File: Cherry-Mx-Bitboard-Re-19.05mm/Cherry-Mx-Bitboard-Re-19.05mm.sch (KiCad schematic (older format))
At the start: 11 parts, among them SW1 SW_Push

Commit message: added choc
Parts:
- added D3, D4: 1N4148W-Diode, Footprints:1N4148W, symbol Cherry-Mx-Bitboard-Re-19.05mm-rescue:1N4148W-Diode
- added SW2: SW_Push-Switch, keyswitches:Kailh_socket_PG1350, symbol Cherry-Mx-Bitboard-Re-19.05mm-rescue:SW_Push-Switch
- Col111, Col112, Col113, Col114, Row111, Row112, Row113, Row114: symbol Connector_Generic:Conn_01x01 -> Cherry-Mx-Bitboard-Re-19.05mm-rescue:Conn_01x01-Connector_Generic
- D1, D2: symbol Diode:1N4148W -> Cherry-Mx-Bitboard-Re-19.05mm-rescue:1N4148W-Diode
- SW1: symbol Switch:SW_Push -> Cherry-Mx-Bitboard-Re-19.05mm-rescue:SW_Push-Switch
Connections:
- wire segments 22 -> 33
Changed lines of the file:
@@
 EESchema Schematic File Version 4
-LIBS:Cherry-Mx-Bitboard-Re-19.05mm-cache
 EELAYER 30 0
 EELAYER END
@@
 $EndDescr
 $Comp
-L Switch:SW_Push SW1
+L Cherry-Mx-Bitboard-Re-19.05mm-rescue:SW_Push-Switch SW1
 U 1 1 5B598EC8
 P 2000 4500
@@
 	1750 4500 1750 4600
 $Comp
-L Connector_Generic:Conn_01x01 Col111
+L Cherry-Mx-Bitboard-Re-19.05mm-rescue:Conn_01x01-Connector_Generic Col111
 U 1 1 5B8A669A
 P 9450 2800
@@
 $EndComp
 $Comp
-L Diode:1N4148W D1
+L Cherry-Mx-Bitboard-Re-19.05mm-rescue:1N4148W-Diode D1
 U 1 1 5B954373
 P 2400 4500
@@
 Row1
 $Comp
-L Connector_Generic:Conn_01x01 Row112
+L Cherry-Mx-Bitboard-Re-19.05mm-rescue:Conn_01x01-Connector_Generic Row112
 U 1 1 5B8A9836
 P 9150 3300
@@
 Row1
 $Comp
-L Connector_Generic:Conn_01x01 Row113
+L Cherry-Mx-Bitboard-Re-19.05mm-rescue:Conn_01x01-Connector_Generic Row113
 U 1 1 5BCDE34F
 P 9950 3100
@@
 $EndComp
 $Comp
-L Connector_Generic:Conn_01x01 Row114
+L Cherry-Mx-Bitboard-Re-19.05mm-rescue:Conn_01x01-Connector_Generic Row114
 U 1 1 5BCDE64E
 P 9950 3300
@@
 $EndComp
 $Comp
-L Connector_Generic:Conn_01x01 Col112
+L Cherry-Mx-Bitboard-Re-19.05mm-rescue:Conn_01x01-Connector_Generic Col112
 U 1 1 5BCE08C8
 P 9650 2800
@@
 Col1
 $Comp
-L Connector_Generic:Conn_01x01 Col113
+L Cherry-Mx-Bitboard-Re-19.05mm-rescue:Conn_01x01-Connector_Generic Col113
 U 1 1 5BD12023
 P 9450 3600
@@
 $EndComp
 $Comp
-L Connector_Generic:Conn_01x01 Col114
+L Cherry-Mx-Bitboard-Re-19.05mm-rescue:Conn_01x01-Connector_Generic Col114
 U 1 1 5BD1233F
 P 9650 3600
@@
 	9350 3200 9750 3200
 $Comp
-L Connector_Generic:Conn_01x01 Row111
+L Cherry-Mx-Bitboard-Re-19.05mm-rescue:Conn_01x01-Connector_Generic Row111
 U 1 1 5B8A59A9
 P 9150 3100
@@
 	2200 4900 2250 4900
 $Comp
-L Diode:1N4148W D2
+L Cherry-Mx-Bitboard-Re-19.05mm-rescue:1N4148W-Diode D2
 U 1 1 5E1FCD4B
 P 2400 4900
@@
 	2550 4900 2750 4900
 Wire Wire Line
-	2200 4900 2200 4500
+	2200 4900 2200 4700
 Connection ~ 2200 4500
 Wire Wire Line
 	2750 4900 2750 4500
 Connection ~ 2750 4500
+$Comp
+L Cherry-Mx-Bitboard-Re-19.05mm-rescue:SW_Push-Switch SW2
+U 1 1 5EAC5567
+P 2000 4700
+F 0 "SW2" H 2000 4985 50  0000 C CNN
+F 1 "SW_Push-Switch" H 2000 4894 50  0000 C CNN
+F 2 "keyswitches:Kailh_socket_PG1350" H 2000 4900 50  0001 C CNN
+F 3 "" H 2000 4900 50  0001 C CNN
+	1    2000 4700
+	1    0    0    -1
+$EndComp
+Connection ~ 2200 4700
+Wire Wire Line
+	2200 4700 2200 4500
+Wire Wire Line
+	1800 4700 1750 4700
+Wire Wire Line
+	1750 4700 1750 4600
+Connection ~ 1750 4600
+$Comp
+L Cherry-Mx-Bitboard-Re-19.05mm-rescue:1N4148W-Diode D3
+U 1 1 5EAE37ED
+P 2400 5250
+F 0 "D3" H 2400 5467 50  0000 C CNN
+F 1 "1N4148W-Diode" H 2400 5376 50  0000 C CNN
+F 2 "Footprints:1N4148W" H 2400 5075 50  0001 C CNN
+F 3 "" H 2400 5250 50  0001 C CNN
+	1    2400 5250
+	-1   0    0    -1
+$EndComp
+Wire Wire Line
+	2550 5250 2750 5250
+Wire Wire Line
+	2750 5250 2750 4900
+Connection ~ 2750 4900
+Wire Wire Line
+	2250 5250 2200 5250
+Wire Wire Line
+	2200 5250 2200 4900
+Connection ~ 2200 4900
+$Comp
+L Cherry-Mx-Bitboard-Re-19.05mm-rescue:1N4148W-Diode D4
+U 1 1 5EAE84E4
+P 2400 5600
+F 0 "D4" H 2400 5817 50  0000 C CNN
+F 1 "1N4148W-Diode" H 2400 5726 50  0000 C CNN
+F 2 "Footprints:1N4148W" H 2400 5425 50  0001 C CNN
+F 3 "" H 2400 5600 50  0001 C CNN
+	1    2400 5600
+	-1   0    0    -1
+$EndComp
+Wire Wire Line
+	2550 5600 2750 5600
+Wire Wire Line
+	2750 5600 2750 5250
+Connection ~ 2750 5250
+Wire Wire Line
+	2250 5600 2200 5600
+Wire Wire Line
+	2200 5600 2200 5250
+Connection ~ 2200 5250
 $EndSCHEMATC

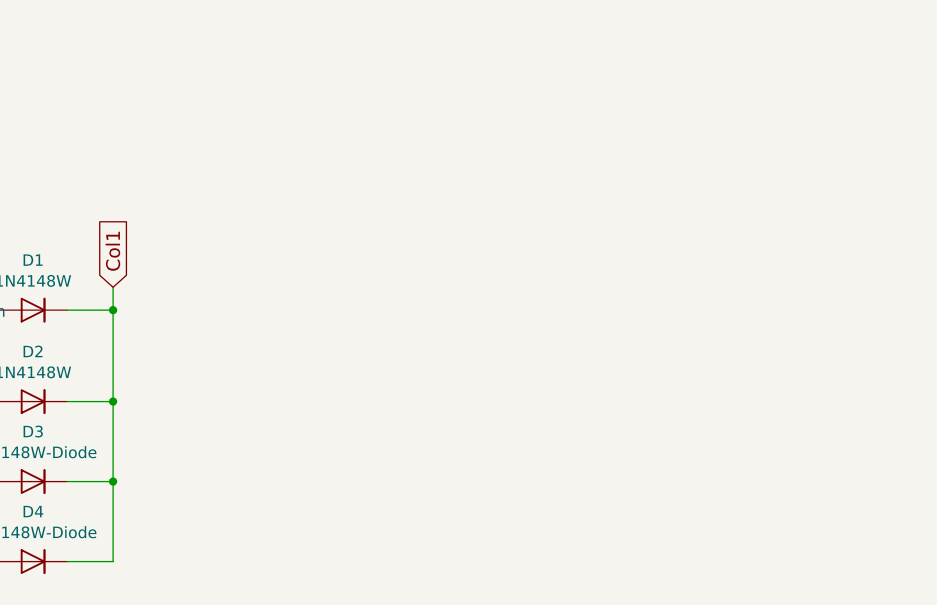
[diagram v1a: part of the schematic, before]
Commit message: add rgb leds
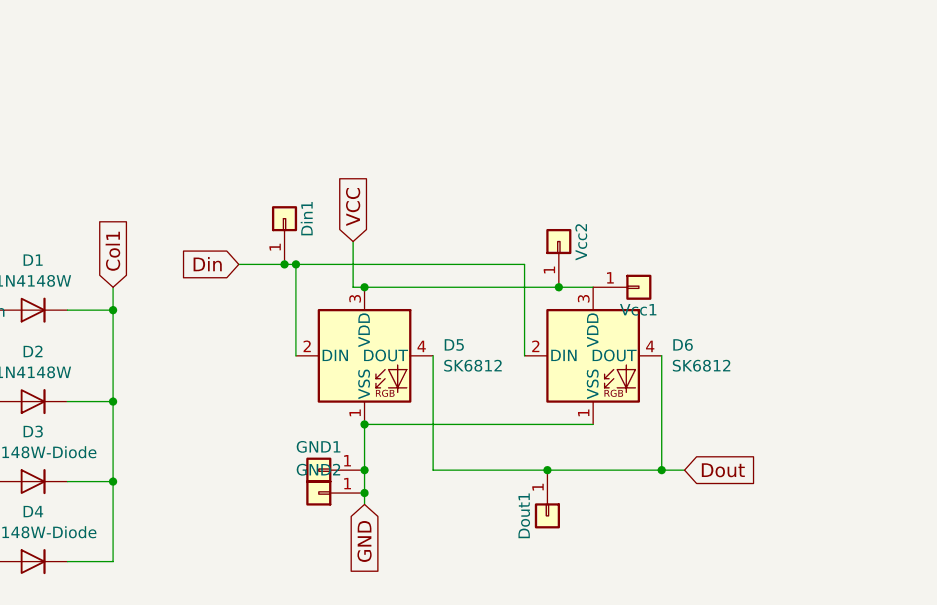
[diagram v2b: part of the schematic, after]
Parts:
- added D5, D6: SK6812, LED_SMD:LED_SK6812_PLCC4_5.0x5.0mm_P3.2mm, symbol LED:SK6812
- added Din1, Dout1, GND1, GND2, Vcc1, Vcc2: Conn_01x01, Footprints:Wirepad, symbol Cherry-Mx-Bitboard-Re-19.05mm-rescue:Conn_01x01-Connector_Generic
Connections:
- new net Din: D5.2 (DIN), D6.2 (DIN), Din1.1 (Pin_1)
- new net Dout: D5.4 (DOUT), D6.4 (DOUT), Dout1.1 (Pin_1)
- new net GND: D5.1 (VSS), D6.1 (VSS), GND1.1 (Pin_1), GND2.1 (Pin_1)
- new net VCC: D5.3 (VDD), D6.3 (VDD), Vcc1.1 (Pin_1), Vcc2.1 (Pin_1)
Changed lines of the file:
@@
 	2200 5600 2200 5250
 Connection ~ 2200 5250
+$Comp
+L LED:SK6812 D5
+U 1 1 5EB32545
+P 3850 4700
+F 0 "D5" H 4194 4746 50  0000 L CNN
+F 1 "SK6812" H 4194 4655 50  0000 L CNN
+F 2 "LED_SMD:LED_SK6812_PLCC4_5.0x5.0mm_P3.2mm" H 3900 4400 50  0001 L TNN
+F 3 "https://cdn-shop.adafruit.com/product-files/1138/SK6812+LED+datasheet+.pdf" H 3950 4325 50  0001 L TNN
+	1    3850 4700
+	1    0    0    -1
+$EndComp
+Text GLabel 3800 4200 1    60   Input ~ 0
+VCC
+Text GLabel 3850 5350 3    60   Input ~ 0
+GND
+Text GLabel 3300 4300 0    60   Input ~ 0
+Din
+Text GLabel 5250 5200 2    60   Input ~ 0
+Dout
+$Comp
+L LED:SK6812 D6
+U 1 1 5EB36B3B
+P 4850 4700
+F 0 "D6" H 5194 4746 50  0000 L CNN
+F 1 "SK6812" H 5194 4655 50  0000 L CNN
+F 2 "LED_SMD:LED_SK6812_PLCC4_5.0x5.0mm_P3.2mm" H 4900 4400 50  0001 L TNN
+F 3 "https://cdn-shop.adafruit.com/product-files/1138/SK6812+LED+datasheet+.pdf" H 4950 4325 50  0001 L TNN
+	1    4850 4700
+	1    0    0    -1
+$EndComp
+Wire Wire Line
+	3800 4200 3800 4400
+Wire Wire Line
+	3800 4400 3850 4400
+Wire Wire Line
+	4850 4400 4700 4400
+Connection ~ 3850 4400
+Wire Wire Line
+	3850 5000 4850 5000
+Wire Wire Line
+	3850 5350 3850 5300
+Connection ~ 3850 5000
+Wire Wire Line
+	3550 4300 3550 4700
+Wire Wire Line
+	3550 4300 4550 4300
+Wire Wire Line
+	4550 4300 4550 4700
+Connection ~ 3550 4300
+Wire Wire Line
+	5150 4700 5150 5200
+Wire Wire Line
+	5150 5200 5250 5200
+Wire Wire Line
+	4150 4700 4150 5200
+Wire Wire Line
+	4150 5200 4650 5200
+Connection ~ 5150 5200
+$Comp
+L Cherry-Mx-Bitboard-Re-19.05mm-rescue:Conn_01x01-Connector_Generic Din1
+U 1 1 5EB414D3
+P 3500 4100
+F 0 "Din1" H 3500 4000 50  0000 C CNN
+F 1 "Conn_01x01" V 3375 4012 50  0001 R CNN
+F 2 "Footprints:Wirepad" H 3500 4100 50  0001 C CNN
+F 3 "~" H 3500 4100 50  0001 C CNN
+	1    3500 4100
+	0    -1   -1   0
+$EndComp
+$Comp
+L Cherry-Mx-Bitboard-Re-19.05mm-rescue:Conn_01x01-Connector_Generic Dout1
+U 1 1 5EB42BEB
+P 4650 5400
+F 0 "Dout1" H 4650 5300 50  0000 C CNN
+F 1 "Conn_01x01" V 4525 5312 50  0001 R CNN
+F 2 "Footprints:Wirepad" H 4650 5400 50  0001 C CNN
+F 3 "~" H 4650 5400 50  0001 C CNN
+	1    4650 5400
+	0    1    1    0
+$EndComp
+$Comp
+L Cherry-Mx-Bitboard-Re-19.05mm-rescue:Conn_01x01-Connector_Generic GND1
+U 1 1 5EB43F3B
+P 3650 5200
+F 0 "GND1" H 3650 5100 50  0000 C CNN
+F 1 "Conn_01x01" V 3525 5112 50  0001 R CNN
+F 2 "Footprints:Wirepad" H 3650 5200 50  0001 C CNN
+F 3 "~" H 3650 5200 50  0001 C CNN
+	1    3650 5200
+	-1   0    0    1
+$EndComp
+$Comp
+L Cherry-Mx-Bitboard-Re-19.05mm-rescue:Conn_01x01-Connector_Generic Vcc1
+U 1 1 5EB45E0D
+P 5050 4400
+F 0 "Vcc1" H 5050 4300 50  0000 C CNN
+F 1 "Conn_01x01" V 4925 4312 50  0001 R CNN
+F 2 "Footprints:Wirepad" H 5050 4400 50  0001 C CNN
+F 3 "~" H 5050 4400 50  0001 C CNN
+	1    5050 4400
+	1    0    0    -1
+$EndComp
+Connection ~ 3850 5200
+Wire Wire Line
+	3850 5200 3850 5000
+Connection ~ 4650 5200
+Wire Wire Line
+	4650 5200 5150 5200
+Wire Wire Line
+	3500 4300 3550 4300
+Wire Wire Line
+	3500 4300 3300 4300
+Connection ~ 3500 4300
+$Comp
+L Cherry-Mx-Bitboard-Re-19.05mm-rescue:Conn_01x01-Connector_Generic GND2
+U 1 1 5EB66F22
+P 3650 5300
+F 0 "GND2" H 3650 5200 50  0000 C CNN
+F 1 "Conn_01x01" V 3525 5212 50  0001 R CNN
+F 2 "Footprints:Wirepad" H 3650 5300 50  0001 C CNN
+F 3 "~" H 3650 5300 50  0001 C CNN
+	1    3650 5300
+	-1   0    0    1
+$EndComp
+$Comp
+L Cherry-Mx-Bitboard-Re-19.05mm-rescue:Conn_01x01-Connector_Generic Vcc2
+U 1 1 5EB69C64
+P 4700 4200
+F 0 "Vcc2" H 4700 4100 50  0000 C CNN
+F 1 "Conn_01x01" V 4575 4112 50  0001 R CNN
+F 2 "Footprints:Wirepad" H 4700 4200 50  0001 C CNN
+F 3 "~" H 4700 4200 50  0001 C CNN
+	1    4700 4200
+	0    -1   -1   0
+$EndComp
+Connection ~ 4700 4400
+Wire Wire Line
+	4700 4400 3850 4400
+Connection ~ 3850 5300
+Wire Wire Line
+	3850 5300 3850 5200
 $EndSCHEMATC

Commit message: simplified
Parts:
- removed D3, D4: 1N4148W-Diode, Footprints:1N4148W, symbol Cherry-Mx-Bitboard-Re-19.05mm-rescue:1N4148W-Diode
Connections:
- net Row1: now also SW1.2, SW2.2; no longer SW1.1, SW2.1
- net at D1.2 (A), D2.2 (A): now also SW1.1, SW2.1; no longer SW1.2, SW2.2
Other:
- moved on the sheet: SW1, SW2
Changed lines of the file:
@@
 L Cherry-Mx-Bitboard-Re-19.05mm-rescue:SW_Push-Switch SW1
 U 1 1 5B598EC8
-P 2000 4500
-F 0 "SW1" H 2000 4785 50  0000 C CNN
-F 1 "SW_Push" H 2000 4694 50  0000 C CNN
-F 2 "Footprints:CherryMx_Socket" H 2000 4700 50  0001 C CNN
-F 3 "" H 2000 4700 50  0001 C CNN
-	1    2000 4500
+P 1800 4350
+F 0 "SW1" H 1800 4635 50  0000 C CNN
+F 1 "SW_Push" H 1800 4544 50  0000 C CNN
+F 2 "Footprints:CherryMx_Socket" H 1800 4550 50  0001 C CNN
+F 3 "" H 1800 4550 50  0001 C CNN
+	1    1800 4350
 	1    0    0    -1
 $EndComp
 Wire Wire Line
 	2200 4500 2250 4500
-Wire Wire Line
-	1800 4500 1750 4500
 Wire Wire Line
 	1750 4500 1750 4600
@@
 	2550 4900 2750 4900
 Wire Wire Line
-	2200 4900 2200 4700
-Connection ~ 2200 4500
-Wire Wire Line
 	2750 4900 2750 4500
 Connection ~ 2750 4500
@@
 L Cherry-Mx-Bitboard-Re-19.05mm-rescue:SW_Push-Switch SW2
 U 1 1 5EAC5567
-P 2000 4700
-F 0 "SW2" H 2000 4985 50  0000 C CNN
-F 1 "SW_Push-Switch" H 2000 4894 50  0000 C CNN
-F 2 "keyswitches:Kailh_socket_PG1350" H 2000 4900 50  0001 C CNN
-F 3 "" H 2000 4900 50  0001 C CNN
-	1    2000 4700
-	1    0    0    -1
-$EndComp
-Connection ~ 2200 4700
-Wire Wire Line
-	2200 4700 2200 4500
-Wire Wire Line
-	1800 4700 1750 4700
+P 1800 4900
+F 0 "SW2" H 1800 5185 50  0000 C CNN
+F 1 "SW_Push-Switch" H 1800 5094 50  0000 C CNN
+F 2 "keyswitches:Kailh_socket_PG1350" H 1800 5100 50  0001 C CNN
+F 3 "" H 1800 5100 50  0001 C CNN
+	1    1800 4900
+	1    0    0    -1
+$EndComp
 Wire Wire Line
 	1750 4700 1750 4600
 Connection ~ 1750 4600
-$Comp
-L Cherry-Mx-Bitboard-Re-19.05mm-rescue:1N4148W-Diode D3
-U 1 1 5EAE37ED
-P 2400 5250
-F 0 "D3" H 2400 5467 50  0000 C CNN
-F 1 "1N4148W-Diode" H 2400 5376 50  0000 C CNN
-F 2 "Footprints:1N4148W" H 2400 5075 50  0001 C CNN
-F 3 "" H 2400 5250 50  0001 C CNN
-	1    2400 5250
-	-1   0    0    -1
-$EndComp
-Wire Wire Line
-	2550 5250 2750 5250
-Wire Wire Line
-	2750 5250 2750 4900
-Connection ~ 2750 4900
-Wire Wire Line
-	2250 5250 2200 5250
-Wire Wire Line
-	2200 5250 2200 4900
-Connection ~ 2200 4900
-$Comp
-L Cherry-Mx-Bitboard-Re-19.05mm-rescue:1N4148W-Diode D4
-U 1 1 5EAE84E4
-P 2400 5600
-F 0 "D4" H 2400 5817 50  0000 C CNN
-F 1 "1N4148W-Diode" H 2400 5726 50  0000 C CNN
-F 2 "Footprints:1N4148W" H 2400 5425 50  0001 C CNN
-F 3 "" H 2400 5600 50  0001 C CNN
-	1    2400 5600
-	-1   0    0    -1
-$EndComp
-Wire Wire Line
-	2550 5600 2750 5600
-Wire Wire Line
-	2750 5600 2750 5250
-Connection ~ 2750 5250
-Wire Wire Line
-	2250 5600 2200 5600
-Wire Wire Line
-	2200 5600 2200 5250
-Connection ~ 2200 5250
 $Comp
 L LED:SK6812 D5
@@
 Wire Wire Line
 	3850 5300 3850 5200
+Wire Wire Line
+	2200 4500 2200 4900
+Wire Wire Line
+	2200 4500 2200 4200
+Wire Wire Line
+	2200 4200 1600 4200
+Wire Wire Line
+	1600 4200 1600 4350
+Connection ~ 2200 4500
+Wire Wire Line
+	2000 4350 2000 4500
+Wire Wire Line
+	1750 4500 2000 4500
+Wire Wire Line
+	2000 4700 2000 4900
+Wire Wire Line
+	1750 4700 2000 4700
+Wire Wire Line
+	1600 4900 1600 5000
+Wire Wire Line
+	1600 5000 2200 5000
+Wire Wire Line
+	2200 5000 2200 4900
+Connection ~ 2200 4900
 $EndSCHEMATC

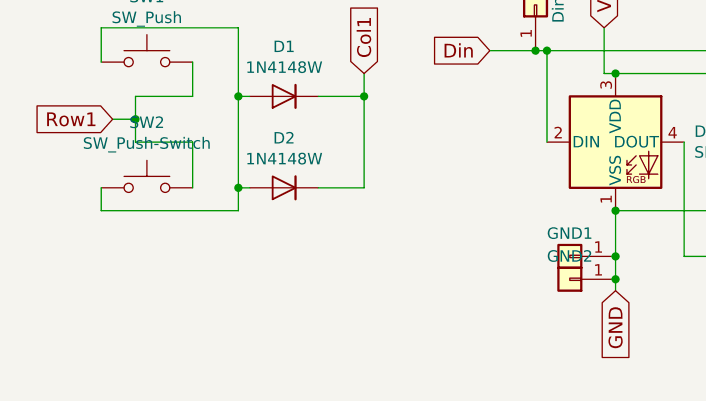
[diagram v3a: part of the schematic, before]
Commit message: fix both sides rgb leds
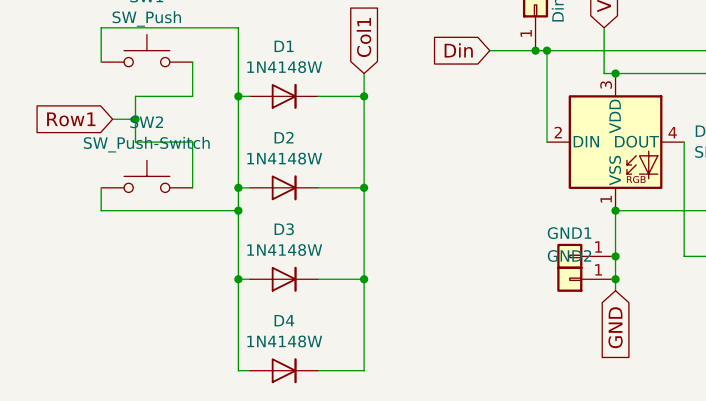
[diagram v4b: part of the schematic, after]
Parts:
- added D3, D4: 1N4148W, Footprints:1N4148W, symbol Cherry-Mx-Bitboard-Re-19.05mm-rescue:1N4148W-Diode
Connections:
- net Col1: now also D3.1 (K), D4.1 (K)
- net at D1.2 (A), D2.2 (A), SW1.1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: now also D3.2 (A), D4.2 (A)
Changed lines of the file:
@@
 	2200 5000 2200 4900
 Connection ~ 2200 4900
+$Comp
+L Cherry-Mx-Bitboard-Re-19.05mm-rescue:1N4148W-Diode D3
+U 1 1 5EB08F87
+P 2400 5300
+F 0 "D3" H 2400 5083 50  0000 C CNN
+F 1 "1N4148W" H 2400 5174 50  0000 C CNN
+F 2 "Footprints:1N4148W" H 2400 5125 50  0001 C CNN
+F 3 "https://www.vishay.com/docs/85748/1n4148w.pdf" H 2400 5300 50  0001 C CNN
+	1    2400 5300
+	-1   0    0    1
+$EndComp
+$Comp
+L Cherry-Mx-Bitboard-Re-19.05mm-rescue:1N4148W-Diode D4
+U 1 1 5EB08F8D
+P 2400 5700
+F 0 "D4" H 2400 5483 50  0000 C CNN
+F 1 "1N4148W" H 2400 5574 50  0000 C CNN
+F 2 "Footprints:1N4148W" H 2400 5525 50  0001 C CNN
+F 3 "https://www.vishay.com/docs/85748/1n4148w.pdf" H 2400 5700 50  0001 C CNN
+	1    2400 5700
+	-1   0    0    1
+$EndComp
+Wire Wire Line
+	2200 5300 2250 5300
+Connection ~ 2200 5000
+Wire Wire Line
+	2200 5000 2200 5300
+Wire Wire Line
+	2200 5300 2200 5700
+Wire Wire Line
+	2200 5700 2250 5700
+Connection ~ 2200 5300
+Wire Wire Line
+	2750 4900 2750 5300
+Wire Wire Line
+	2750 5300 2550 5300
+Connection ~ 2750 4900
+Wire Wire Line
+	2750 5300 2750 5700
+Wire Wire Line
+	2750 5700 2550 5700
+Connection ~ 2750 5300
 $EndSCHEMATC

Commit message: add custom footprint
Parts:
- D5, D6: footprint LED_SMD:LED_SK6812_PLCC4_5.0x5.0mm_P3.2mm -> customs:LED_SK6812_PLCC4_5.0x5.0mm_P3.2mm_FLIP
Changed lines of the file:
@@
 F 0 "D5" H 4194 4746 50  0000 L CNN
 F 1 "SK6812" H 4194 4655 50  0000 L CNN
-F 2 "LED_SMD:LED_SK6812_PLCC4_5.0x5.0mm_P3.2mm" H 3900 4400 50  0001 L TNN
+F 2 "customs:LED_SK6812_PLCC4_5.0x5.0mm_P3.2mm_FLIP" H 3900 4400 50  0001 L TNN
 F 3 "https://cdn-shop.adafruit.com/product-files/1138/SK6812+LED+datasheet+.pdf" H 3950 4325 50  0001 L TNN
 	1    3850 4700
@@
 F 0 "D6" H 5194 4746 50  0000 L CNN
 F 1 "SK6812" H 5194 4655 50  0000 L CNN
-F 2 "LED_SMD:LED_SK6812_PLCC4_5.0x5.0mm_P3.2mm" H 4900 4400 50  0001 L TNN
+F 2 "customs:LED_SK6812_PLCC4_5.0x5.0mm_P3.2mm_FLIP" H 4900 4400 50  0001 L TNN
 F 3 "https://cdn-shop.adafruit.com/product-files/1138/SK6812+LED+datasheet+.pdf" H 4950 4325 50  0001 L TNN
 	1    4850 4700

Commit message: switch to sk6812 mini-e
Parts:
- removed D5, D6: SK6812, customs:LED_SK6812_PLCC4_5.0x5.0mm_P3.2mm_FLIP, symbol LED:SK6812
- added D5, D6: SK6812MINI_E, customs:YS-SK6812MINI-E_REVERSE, symbol customs:SK6812MINI_E
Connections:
- net Din: now also D5.4 (DIN), D6.4 (DIN)
- net Dout: now also D5.2 (DOUT), D6.2 (DOUT)
- net GND: now also D5.3 (VSS), D6.3 (VSS)
- net VCC: now also D5.1 (VDD), D6.1 (VDD)
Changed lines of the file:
@@
 EESchema Schematic File Version 4
+LIBS:Cherry-Mx-Bitboard-Re-19.05mm-cache
 EELAYER 30 0
 EELAYER END
@@
 	1750 4700 1750 4600
 Connection ~ 1750 4600
-$Comp
-L LED:SK6812 D5
-U 1 1 5EB32545
-P 3850 4700
-F 0 "D5" H 4194 4746 50  0000 L CNN
-F 1 "SK6812" H 4194 4655 50  0000 L CNN
-F 2 "customs:LED_SK6812_PLCC4_5.0x5.0mm_P3.2mm_FLIP" H 3900 4400 50  0001 L TNN
-F 3 "https://cdn-shop.adafruit.com/product-files/1138/SK6812+LED+datasheet+.pdf" H 3950 4325 50  0001 L TNN
-	1    3850 4700
-	1    0    0    -1
-$EndComp
 Text GLabel 3800 4200 1    60   Input ~ 0
 VCC
@@
 Text GLabel 5250 5200 2    60   Input ~ 0
 Dout
-$Comp
-L LED:SK6812 D6
-U 1 1 5EB36B3B
-P 4850 4700
-F 0 "D6" H 5194 4746 50  0000 L CNN
-F 1 "SK6812" H 5194 4655 50  0000 L CNN
-F 2 "customs:LED_SK6812_PLCC4_5.0x5.0mm_P3.2mm_FLIP" H 4900 4400 50  0001 L TNN
-F 3 "https://cdn-shop.adafruit.com/product-files/1138/SK6812+LED+datasheet+.pdf" H 4950 4325 50  0001 L TNN
-	1    4850 4700
-	1    0    0    -1
-$EndComp
 Wire Wire Line
 	3800 4200 3800 4400
 Wire Wire Line
-	3800 4400 3850 4400
-Wire Wire Line
 	4850 4400 4700 4400
-Connection ~ 3850 4400
 Wire Wire Line
 	3850 5000 4850 5000
 Wire Wire Line
 	3850 5350 3850 5300
-Connection ~ 3850 5000
 Wire Wire Line
 	3550 4300 3550 4700
@@
 $EndComp
 Connection ~ 4700 4400
-Wire Wire Line
-	4700 4400 3850 4400
 Connection ~ 3850 5300
 Wire Wire Line
@@
 	2750 5700 2550 5700
 Connection ~ 2750 5300
+$Comp
+L customs:SK6812MINI_E D5
+U 1 1 5ED8CEFA
+P 3850 4700
+F 0 "D5" H 4194 4746 50  0000 L CNN
+F 1 "SK6812MINI_E" H 4194 4655 50  0000 L CNN
+F 2 "customs:YS-SK6812MINI-E_REVERSE" H 3900 4400 50  0001 L TNN
+F 3 "" H 3950 4325 50  0001 L TNN
+	1    3850 4700
+	1    0    0    -1
+$EndComp
+$Comp
+L customs:SK6812MINI_E D6
+U 1 1 5ED8E320
+P 4850 4700
+F 0 "D6" H 5194 4746 50  0000 L CNN
+F 1 "SK6812MINI_E" H 5194 4655 50  0000 L CNN
+F 2 "customs:YS-SK6812MINI-E_REVERSE" H 4900 4400 50  0001 L TNN
+F 3 "" H 4950 4325 50  0001 L TNN
+	1    4850 4700
+	1    0    0    -1
+$EndComp
+Wire Wire Line
+	3800 4400 3850 4400
+Connection ~ 3850 4400
+Wire Wire Line
+	3850 4400 4700 4400
+Connection ~ 3850 5000
+Connection ~ 4850 4400
 $EndSCHEMATC
